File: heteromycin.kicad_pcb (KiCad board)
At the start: 4 copper layers, 200 x 100 mm, 373 parts, among them J1 920-0135-01, J10 Micro_SD_Card_Det_Hirose_DM3AT, J11 20021121-00010C4LF, J12 70543-0001, J13 70543-0001, J14 70543-0001, J15 70543-0001, J16 70543-0001, J17 70543-0001, J18 70543-0001, J19 70543-0001, J2 4DB-P108-06, J20 70543-0003, J21 70543-0002, J22 70543-0002, J23 70543-0002, J24 Conn_02x20_Odd_Even, J3 39531-1002, J4 39531-1002, J5 70543-0003, J6 70543-0003, J7 70543-0003, J8 70543-0003, J9 70543-0003, Q1 DMMT5401, Q10 PMPB20EN, Q11 PSMN1R2-30YLC,115, Q12 PSMN1R2-30YLC,115, Q13 PSMN1R2-30YLC,115, Q14 PMPB20EN, Q15 PMPB20EN, Q16 PMPB20EN, Q17 PMPB20EN, Q18 PMPB20EN, Q19 PMPB20EN, Q2 DMG2305UX, Q20 PMPB20EN, Q21 PMPB20EN, Q22 PMPB20EN, Q23 PMPB20EN, Q24 PMPB20EN, Q25 PMPB20EN, Q26 PMPB20EN, Q27 PMPB20EN, Q28 PMPB20EN, Q29 PMPB20EN, Q3 PMPB20EN, Q30 PMPB20EN, Q31 PMPB20EN, Q32 PMPB20EN, Q33 PMPB20EN, Q34 PMPB20EN, Q35 PMPB20EN, Q36 PMPB20EN, Q37 PMPB20EN, Q38 PMPB20EN, Q39 PMPB20EN, Q4 PMPB20EN, Q40 PMPB20EN, Q41 PMPB20EN, Q42 PMPB20EN, Q43 PMPB20EN, Q44 PMPB20EN, Q45 PMPB20EN, Q46 PMPB20EN, Q47 PMPB20EN, Q48 PMPB20EN, Q49 PMPB20EN, Q5 PMPB20EN, Q6 PMPB20EN, Q7 PMPB20EN, Q8 PMPB20EN, Q9 PMPB20EN, SW1 PTS645VL39-2, U1 CAT24C32, U10 TMC2160-TA, U2 i3A, U3 AP2112K-3.3TRG1, U4 CAT24C32, U5 STM32F765VIT6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

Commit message: Change default SOT1220 MOSFET and added parts alternatives
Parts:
- Q10, Q18, Q19, Q20, Q21, Q22, Q23, Q24, Q25, Q26, Q27, Q28, Q29, Q3, Q30, Q31, Q32, Q33, Q34, Q35, Q36, Q37, Q38, Q39, Q4, Q40, Q41, Q42, Q43, Q44, Q45, Q46, Q47, Q48, Q49, Q5, Q6, Q7, Q8, Q9: value PMPB20EN -> PMPB11EN

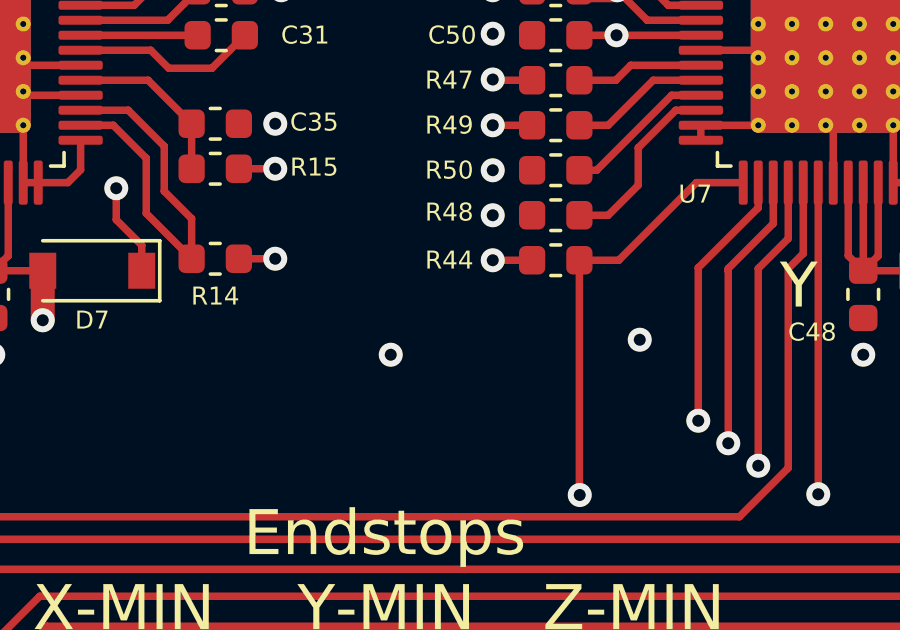
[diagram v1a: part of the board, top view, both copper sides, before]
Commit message: Add drawings and another mounting hole
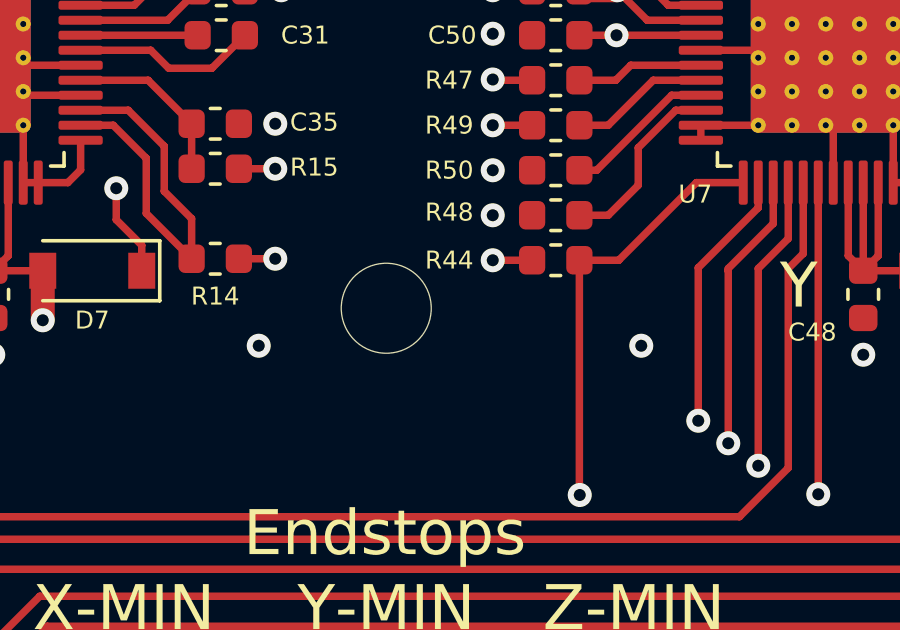
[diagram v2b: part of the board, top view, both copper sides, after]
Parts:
- added H7: 3mm_Mounting_Hole, heteromycin:MountingHole_3mm, F.Cu at (144.5, 89.0)

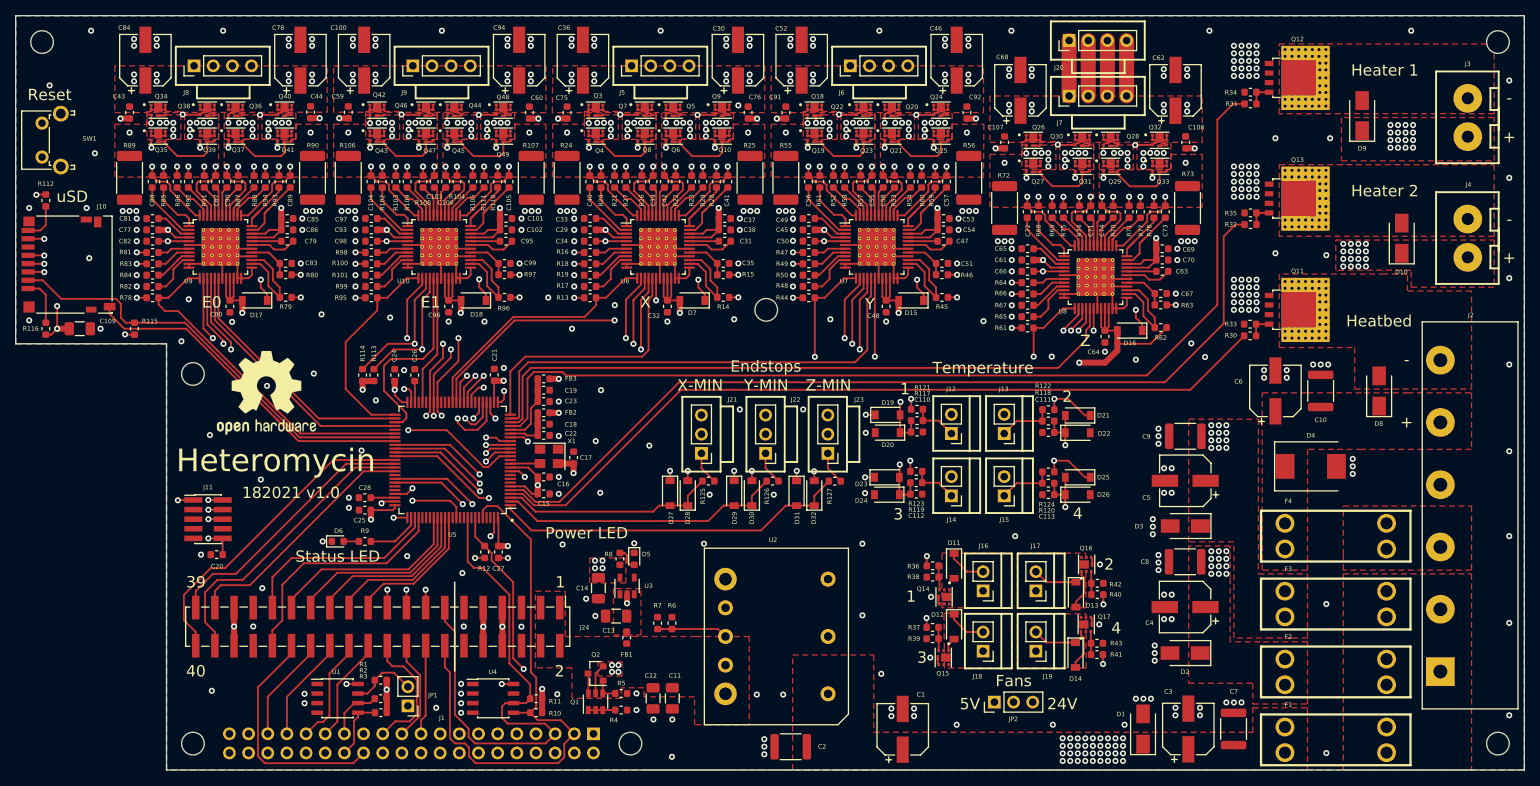
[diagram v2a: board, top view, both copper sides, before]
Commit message: Change mounting holes
Pi mounting holes: M2.5
Board mounting holes: M3

Added a mounting hole near the board center
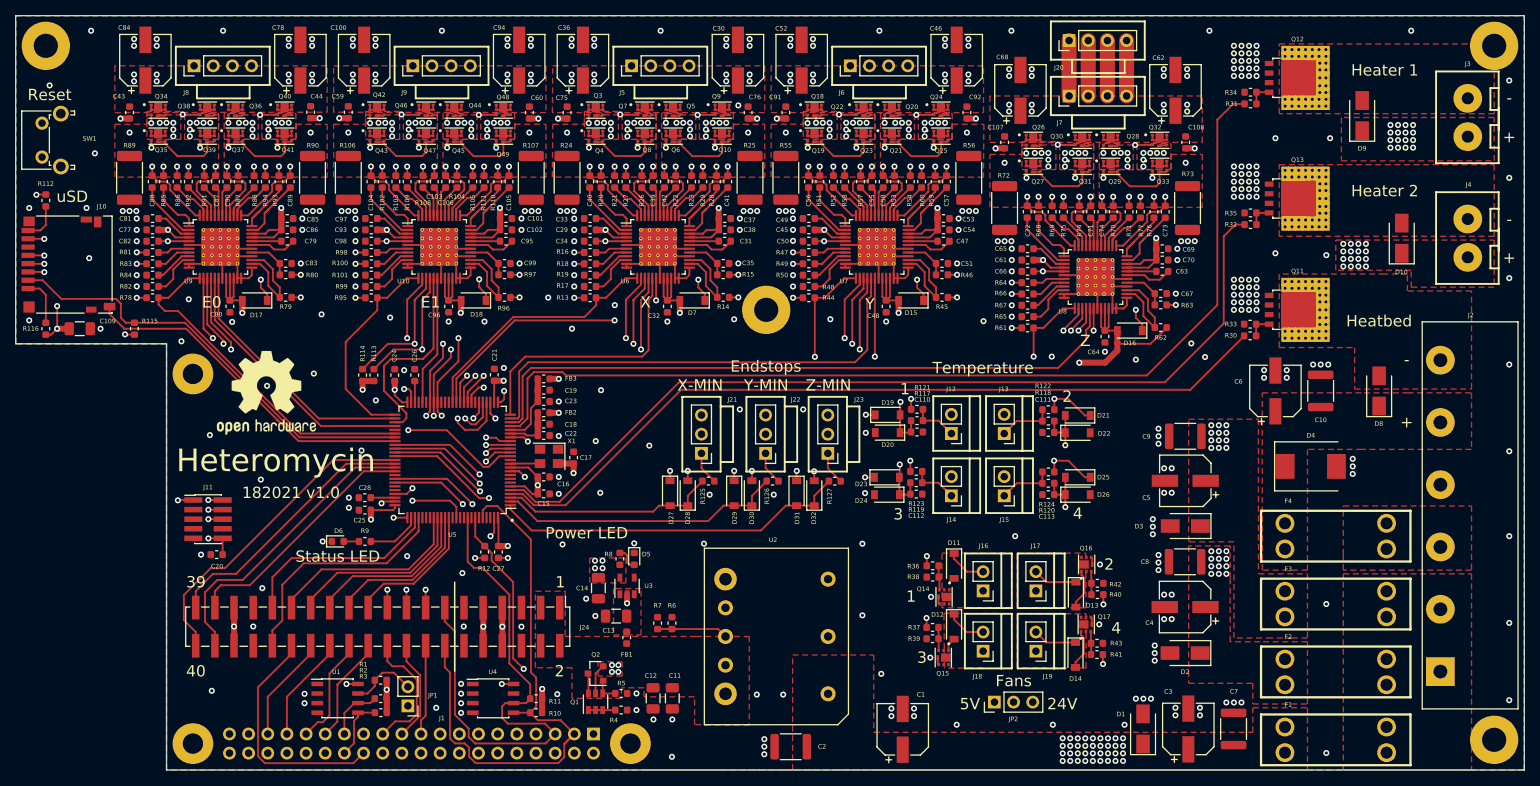
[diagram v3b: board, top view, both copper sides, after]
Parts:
- H1, H2, H4: value 3mm_Mounting_Hole -> MountingHole_2.7mm_M2.5_Pad; footprint heteromycin:MountingHole_3mm -> heteromycin:MountingHole_2.7mm_M2.5_Pad
- H3, H5, H6, H7: value 3mm_Mounting_Hole -> MountingHole_3.2mm_M3_Pad; footprint heteromycin:MountingHole_3mm -> heteromycin:MountingHole_3.2mm_M3_Pad
- moved H3 0.71 mm to (241.0, 54.0)
- moved H5 0.71 mm to (49.0, 54.0)
- moved H6 0.71 mm to (241.0, 146.0)
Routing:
- net /Connectors/SDA: track 76.0 -> 77.9 mm

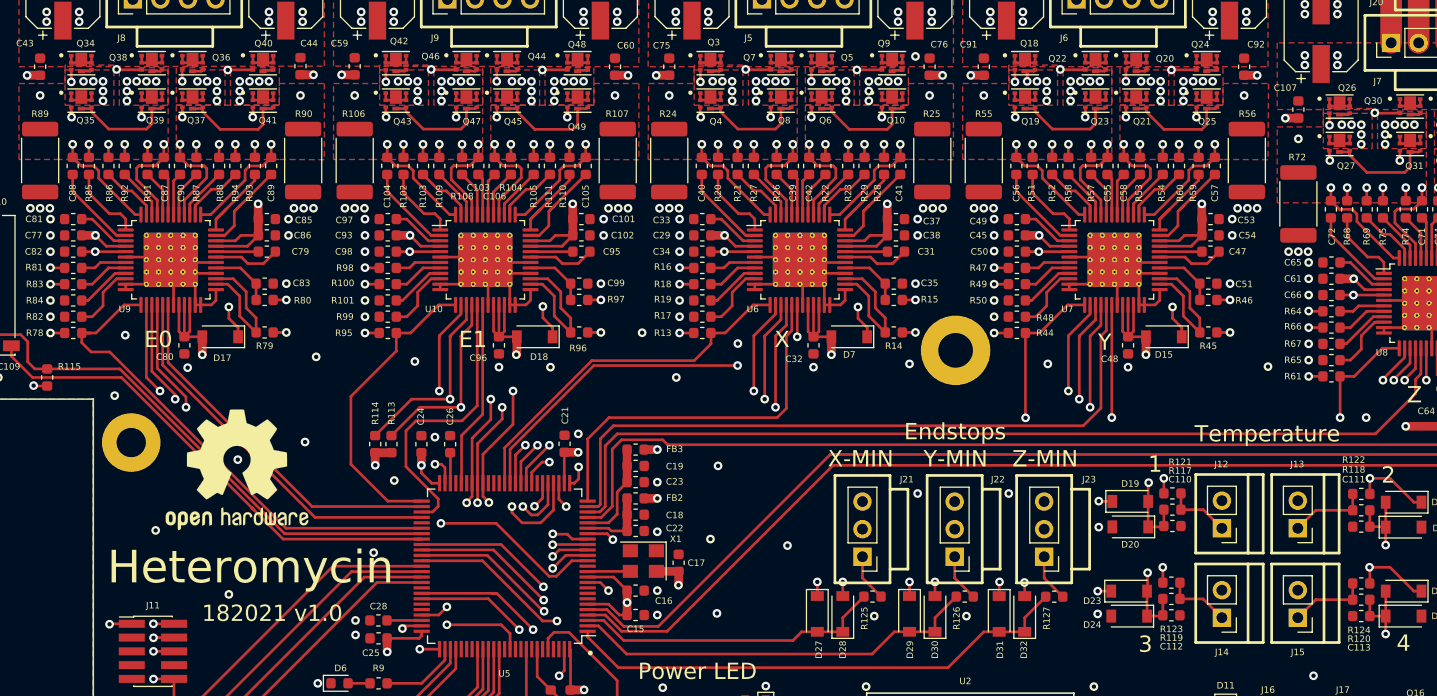
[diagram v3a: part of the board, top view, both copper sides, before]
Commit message: Update image and corrected some copper pure
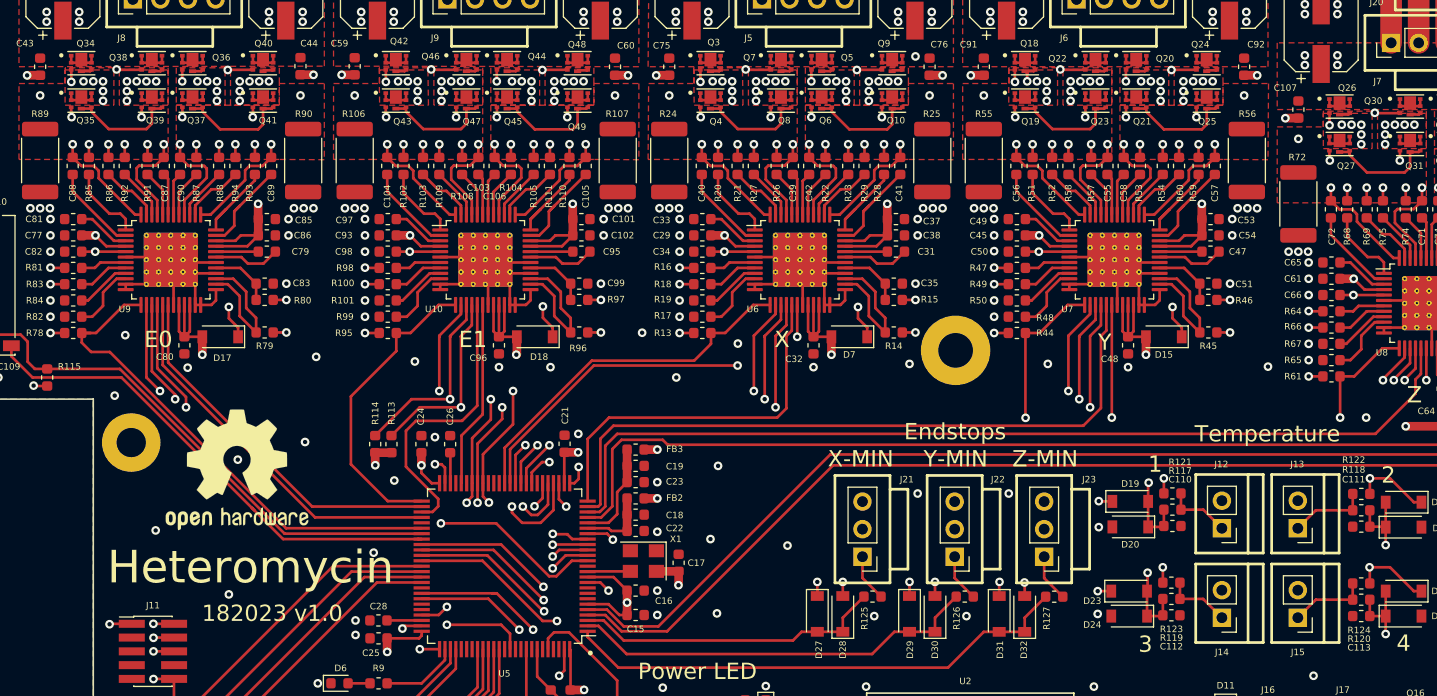
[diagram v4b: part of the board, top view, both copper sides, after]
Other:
- board text added: "182023 v1.0"
- board text removed: "182021 v1.0"
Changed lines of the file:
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@@
     (effects (font (size 1.5 1.5) (thickness 0.3)))
   )
-  (gr_text "182021 v1.0" (at 81.5 113.25) (layer F.SilkS)
+  (gr_text "182023 v1.0" (at 81.5 113.25) (layer F.SilkS)
     (effects (font (size 1.5 1.5) (thickness 0.3)))
   )
@@
     (polygon
       (pts
-        (xy 95.9 62.7) (xy 91.4 62.7) (xy 91.4 66.4) (xy 95.9 66.4)
+        (xy 95.85 62.95) (xy 91.35 62.95) (xy 91.4 66.4) (xy 95.9 66.4)
       )
     )
@@
     (polygon
       (pts
-        (xy 77.15 63.15) (xy 75.3 63.15) (xy 75.3 62.95) (xy 72.65 62.95) (xy 72.65 66.4)
+        (xy 77.15 63.15) (xy 77.15 62.95) (xy 75.3 62.95) (xy 72.65 62.95) (xy 72.65 66.4)
         (xy 77.15 66.4)
       )
@@
     (polygon
       (pts
-        (xy 66.9 62.7) (xy 62.4 62.7) (xy 62.4 66.4) (xy 66.9 66.4)
+        (xy 66.9 62.95) (xy 62.4 62.95) (xy 62.4 66.4) (xy 66.9 66.4)
       )
     )
@@
     (polygon
       (pts
-        (xy 182.9 66.7) (xy 178.4 66.7) (xy 178.4 70.4) (xy 182.9 70.4)
+        (xy 182.9 66.95) (xy 178.4 66.95) (xy 178.4 70.4) (xy 182.9 70.4)
       )
     )
@@
     (polygon
       (pts
-        (xy 153.9 62.7) (xy 149.4 62.7) (xy 149.4 66.4) (xy 153.9 66.4)
+        (xy 153.9 62.95) (xy 149.4 62.95) (xy 149.4 66.4) (xy 153.9 66.4)
       )
     )
@@
     (polygon
       (pts
-        (xy 124.9 62.7) (xy 120.4 62.7) (xy 120.4 66.4) (xy 124.9 66.4)
+        (xy 124.85 62.95) (xy 120.35 62.95) (xy 120.4 66.4) (xy 124.9 66.4)
       )
     )

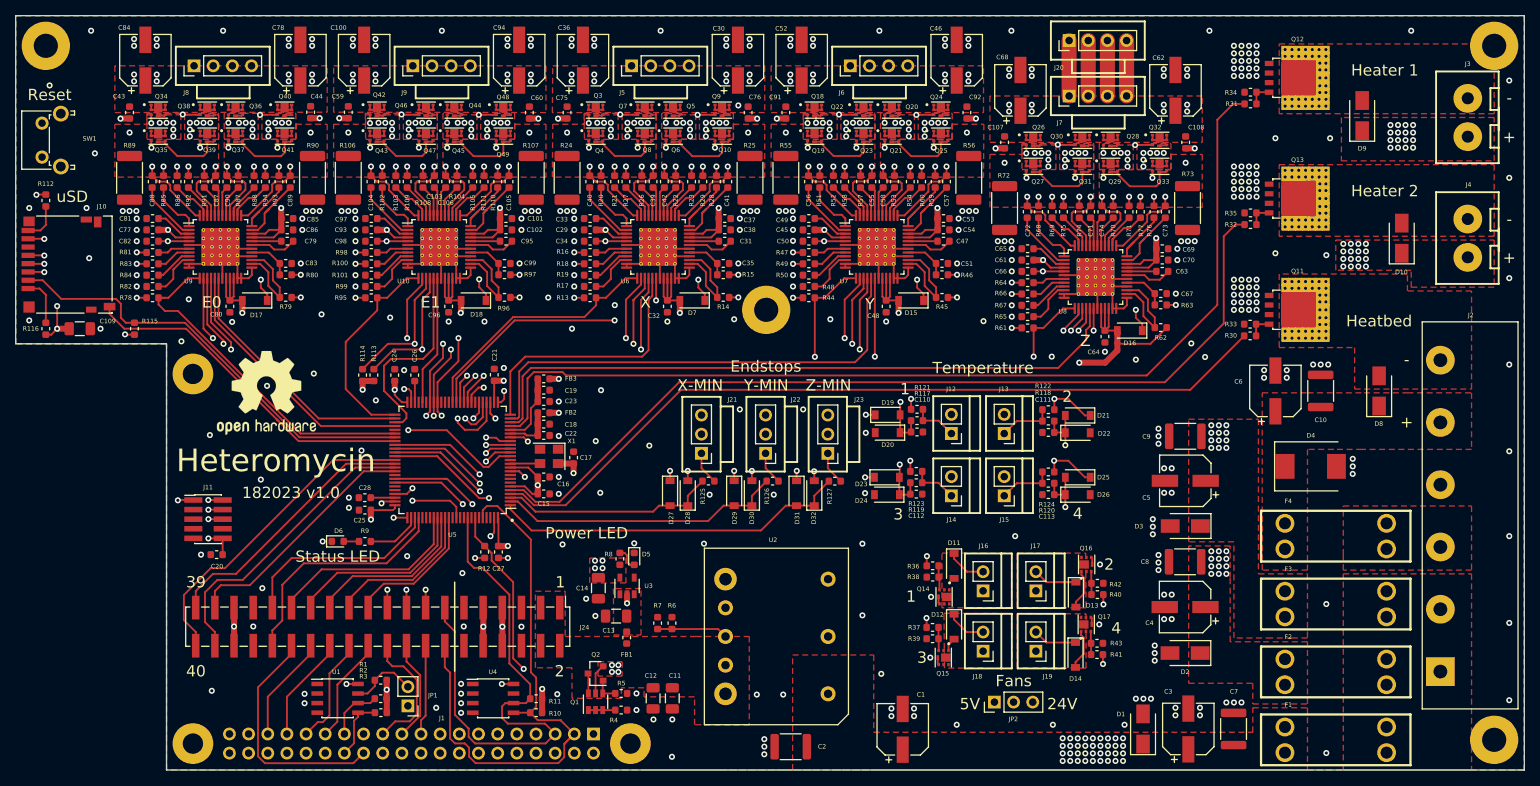
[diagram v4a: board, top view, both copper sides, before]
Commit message: Add bypass cap for I2C EEPROMs and redone some copper pour
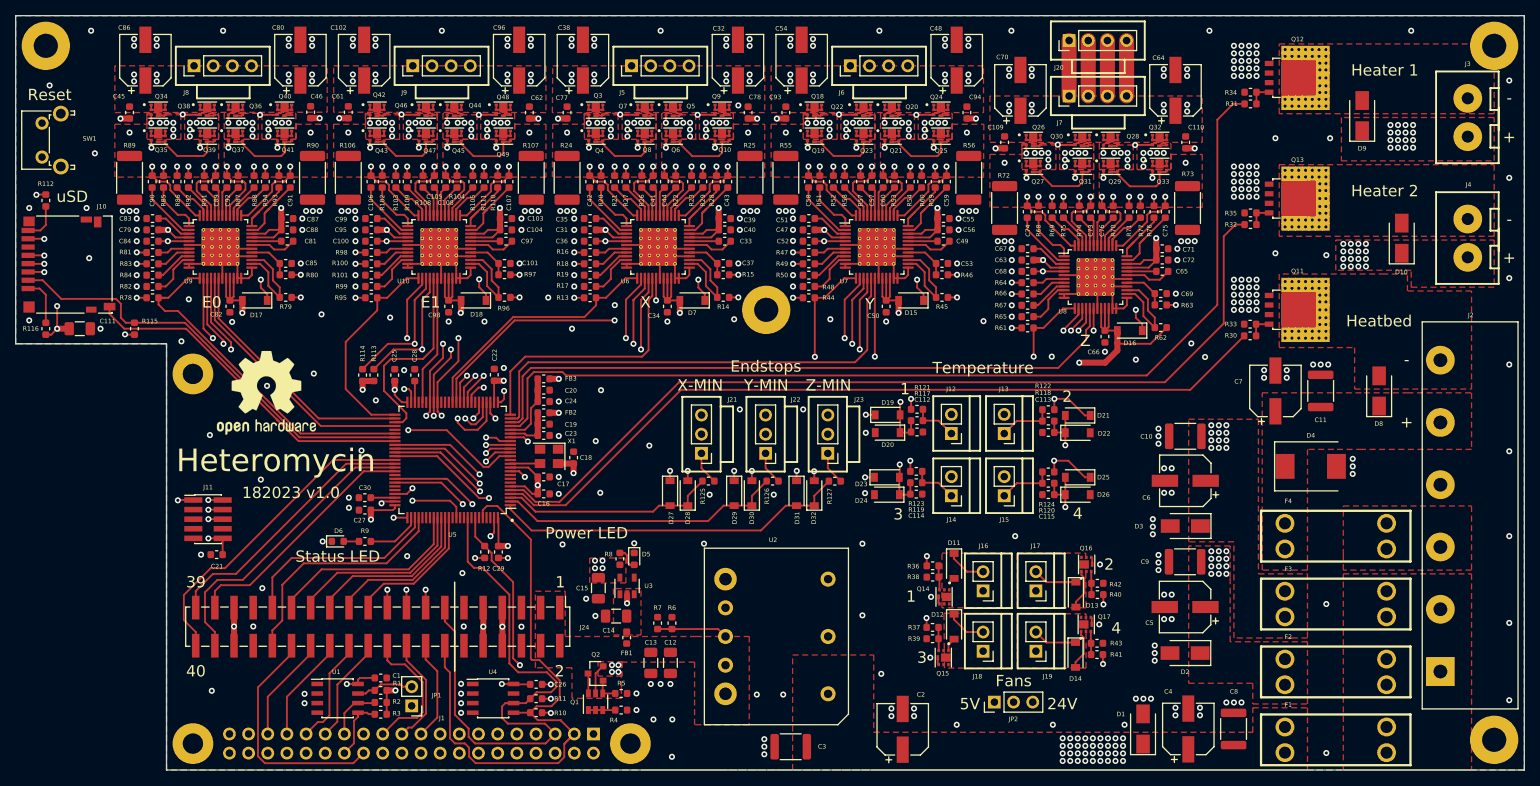
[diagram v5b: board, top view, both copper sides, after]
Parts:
- added C1: 100nF, Capacitor_SMD:C_0603_1608Metric, F.Cu at (93.4, 137.8)
- added C26: 100nF, Capacitor_SMD:C_0603_1608Metric, F.Cu at (114.0, 138.7)
- moved C13 4.71 mm to (129.2, 135.8)
- moved C12 4.71 mm to (131.8, 135.8)
- moved R1 1.35 mm to (93.4, 139.4)
- moved R2 0.50 mm to (93.4, 141.1)
- moved JP1 0.50 mm to (97.5, 141.5)
- moved R3 0.21 mm to (93.4, 142.6)
- renumbered C9 to C10, C98 to C100, C99 to C101, C100 to C102, C101 to C103, C102 to C104, C103 to C105, C104 to C106, C105 to C107, C106 to C108, C107 to C109, C10 to C11, C108 to C110, C109 to C111, C110 to C112, C111 to C113, C112 to C114, C113 to C115, C11 to C12, C12 to C13, C13 to C14, C14 to C15, C15 to C16, C16 to C17, C17 to C18, C18 to C19, C1 to C2, C19 to C20, C20 to C21, C21 to C22, C22 to C23, C23 to C24, C24 to C25, C25 to C27, C26 to C28, C27 to C29, C2 to C3, C28 to C30, C29 to C31, C30 to C32, C31 to C33, C32 to C34, C33 to C35, C34 to C36, C35 to C37, C36 to C38, C37 to C39, C3 to C4, C38 to C40, C39 to C41, C40 to C42, C41 to C43, C42 to C44, C43 to C45, C44 to C46, C45 to C47, C46 to C48, C47 to C49, C4 to C5, C48 to C50, C49 to C51, C50 to C52, C51 to C53, C52 to C54, C53 to C55, C54 to C56, C55 to C57, C56 to C58, C57 to C59, C5 to C6, C58 to C60, C59 to C61, C60 to C62, C61 to C63, C62 to C64, C63 to C65, C64 to C66, C65 to C67, C66 to C68, C67 to C69, C6 to C7, C68 to C70, C69 to C71, C70 to C72, C71 to C73, C72 to C74, C73 to C75, C74 to C76, C75 to C77, C76 to C78, C77 to C79, C7 to C8, C78 to C80, C79 to C81, C80 to C82, C81 to C83, C82 to C84, C83 to C85, C84 to C86, C85 to C87, C86 to C88, C87 to C89, C8 to C9, C88 to C90, C89 to C91, C90 to C92, C91 to C93, C92 to C94, C93 to C95, C94 to C96, C95 to C97, C96 to C98, C97 to C99, H4 to H3, H3 to H4, H6 to H5, H5 to H6
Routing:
- net /Connectors/SCL: track 72.5 -> 78.7 mm
- net VDD3V3: track 195.6 -> 199.9 mm, vias 49 -> 50
- net /Connectors/SDA: track 77.9 -> 82.2 mm
- net /Raspberry Pi Connector/MISO: track 63.7 -> 66.5 mm
- net /Connectors/PI_SCK: track 71.9 -> 73.5 mm
- net /Raspberry Pi Connector/MOSI: track 59.1 -> 60.3 mm
- net Net-(JP1-Pad2): track 8.99 -> 7.75 mm
- net GND: track 163.7 -> 164.9 mm, vias 352 -> 354

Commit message: Fix MOSFET selection
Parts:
- Q14, Q15, Q16, Q17: value PMPB20EN -> PMPB11EN
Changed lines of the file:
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@@
       (effects (font (size 0.6 0.6) (thickness 0.1)))
     )
-    (fp_text value PMPB20EN (at -0.48468 1.89948 270) (layer F.CrtYd)
+    (fp_text value PMPB11EN (at -0.48468 1.89948 270) (layer F.CrtYd)
       (effects (font (size 0.6 0.6) (thickness 0.1)))
     )
@@
       (effects (font (size 0.6 0.6) (thickness 0.1)))
     )
-    (fp_text value PMPB20EN (at 0 1.9 270) (layer F.CrtYd)
+    (fp_text value PMPB11EN (at 0 1.9 270) (layer F.CrtYd)
       (effects (font (size 0.6 0.6) (thickness 0.1)))
     )
@@
       (effects (font (size 0.6 0.6) (thickness 0.1)))
     )
-    (fp_text value PMPB20EN (at -0.48468 1.89948 90) (layer F.CrtYd)
+    (fp_text value PMPB11EN (at -0.48468 1.89948 90) (layer F.CrtYd)
       (effects (font (size 0.6 0.6) (thickness 0.1)))
     )
@@
       (effects (font (size 0.6 0.6) (thickness 0.1)))
     )
-    (fp_text value PMPB20EN (at -0.48468 1.89948 90) (layer F.CrtYd)
+    (fp_text value PMPB11EN (at -0.48468 1.89948 90) (layer F.CrtYd)
       (effects (font (size 0.6 0.6) (thickness 0.1)))
     )
